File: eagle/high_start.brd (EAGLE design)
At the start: 100.1 x 80.8 mm, 34 parts, among them IC1 7805L, Q1 16Mhz, Q2 IRF510, Q3 IRF510, Q4 IRF510, U2 ATMEGA328P_PDIP

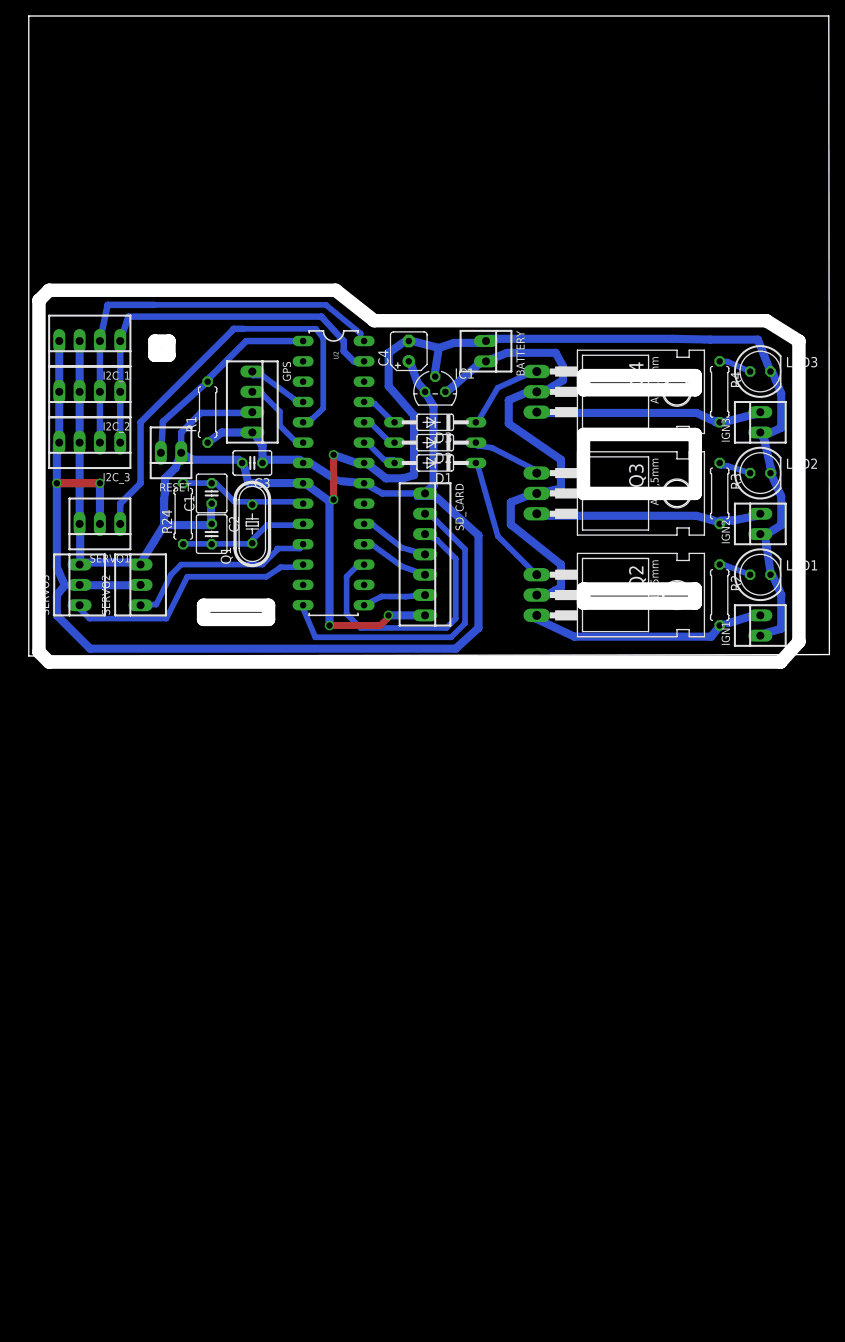
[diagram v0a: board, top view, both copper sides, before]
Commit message: pulldown resistors onto schemo
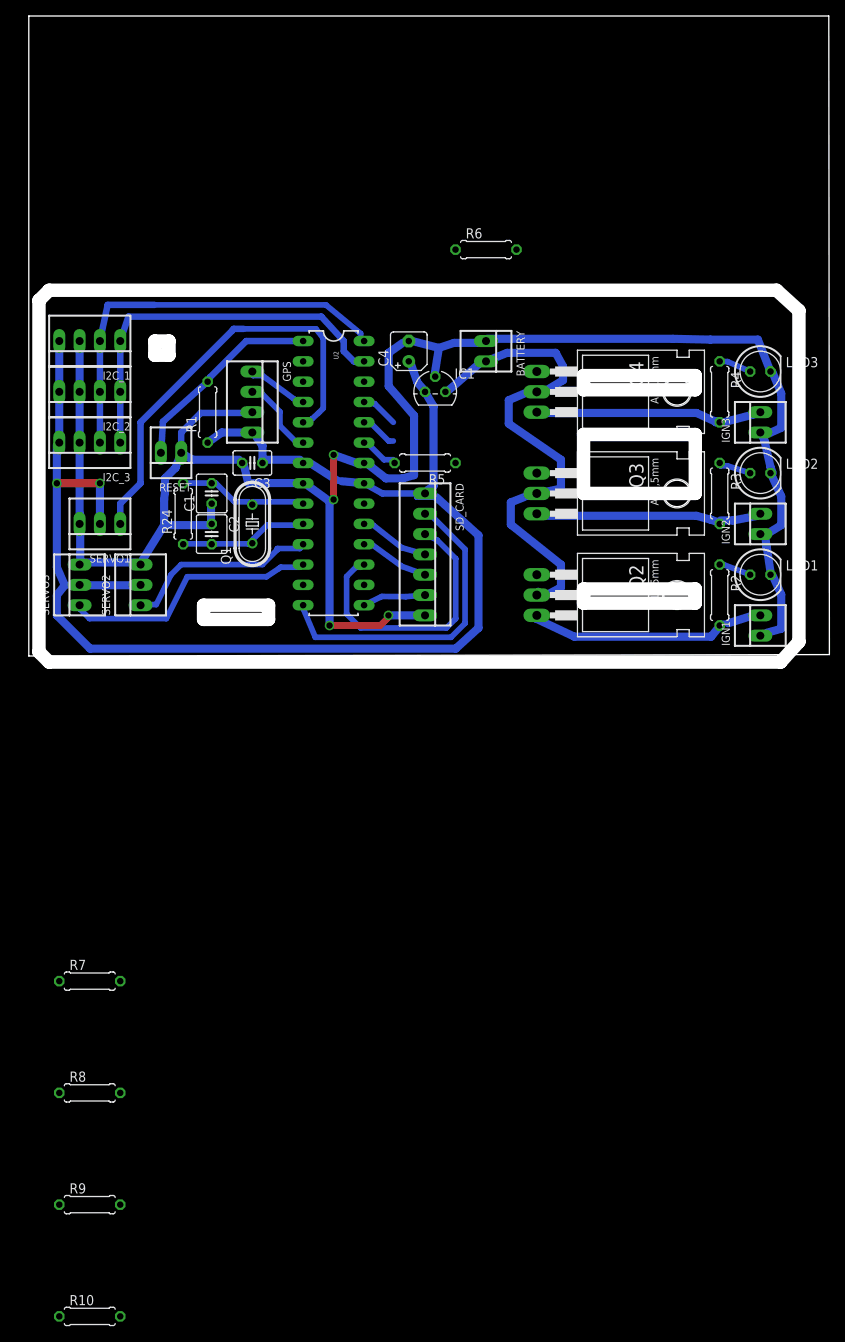
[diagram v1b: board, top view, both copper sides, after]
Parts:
- removed D1, D2, D3: 1N4148DO35-10, diode:DO35-10
- added R10, R6, R9: 10k, rcl:0207/7
- added R5, R7, R8: 220, rcl:0207/7
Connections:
- net GND: now also R10.2, R6.2, R9.2
- net N$12: now also Q2.1, R5.1; no longer D2.C, Q3.1
- net N$13: now also Q3.1, R7.1; no longer D1.C, Q2.1
- net N$14: now also R8.1; no longer D3.C
- net N$18: now also R10.1, R5.2; no longer D1.A
- net N$19: now also R7.2, R9.1; no longer D2.A
- net N$20: now also R6.1, R8.2; no longer D3.A
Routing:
- net N$13: track 16.5 -> 0.00 mm
- net N$14: track 10.5 -> 0.00 mm
- net N$12: track 8.75 -> 0.00 mm
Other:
- outline, holes or cut-outs redrawn
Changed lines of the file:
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@@
 <?xml version="1.0" encoding="utf-8"?>
 <!DOCTYPE eagle SYSTEM "eagle.dtd">
-<eagle version="7.6.0">
+<eagle version="7.7.0">
 <drawing>
 <settings>
@@
 <wire x1="2.54" y1="-0.762" x2="93.98" y2="-0.762" width="1.6764" layer="46"/>
 <wire x1="93.98" y1="-0.762" x2="96.266" y2="1.778" width="1.6764" layer="46"/>
-<wire x1="96.266" y1="1.778" x2="96.266" y2="39.37" width="1.6764" layer="46"/>
-<wire x1="96.266" y1="39.37" x2="92.202" y2="41.91" width="1.6764" layer="46"/>
-<wire x1="92.202" y1="41.91" x2="43.18" y2="41.91" width="1.6764" layer="46"/>
-<wire x1="43.18" y1="41.91" x2="38.354" y2="45.72" width="1.6764" layer="46"/>
-<wire x1="38.354" y1="45.72" x2="2.54" y2="45.72" width="1.6764" layer="46"/>
+<wire x1="96.266" y1="1.778" x2="96.266" y2="43.18" width="1.6764" layer="46"/>
+<wire x1="96.266" y1="43.18" x2="93.472" y2="45.72" width="1.6764" layer="46"/>
+<wire x1="93.472" y1="45.72" x2="2.54" y2="45.72" width="1.6764" layer="46"/>
 <wire x1="1.27" y1="44.45" x2="2.54" y2="45.72" width="1.6764" layer="46"/>
 <wire x1="69.342" y1="27.686" x2="69.342" y2="20.32" width="1.6764" layer="46"/>
@@
 <element name="Q2" library="transistor-fet" package="TO220" value="IRF510" x="69.85" y="7.62" rot="R270"/>
 <element name="Q3" library="transistor-fet" package="TO220" value="IRF510" x="69.85" y="20.32" rot="R270"/>
-<element name="D1" library="diode" package="DO35-10" value="1N4148DO35-10" x="50.8" y="24.13" rot="R180"/>
-<element name="D2" library="diode" package="DO35-10" value="1N4148DO35-10" x="50.8" y="26.67" rot="R180"/>
 <element name="Q4" library="transistor-fet" package="TO220" value="IRF510" x="69.85" y="33.02" rot="R270"/>
-<element name="D3" library="diode" package="DO35-10" value="1N4148DO35-10" x="50.8" y="29.21" rot="R180"/>
 <element name="SERVO1" library="con-molex" package="22-23-2031" value="22-23-2031" x="8.89" y="16.51" rot="R180">
 <attribute name="OC_NEWARK" value="30C0862" x="8.89" y="16.51" size="1.778" layer="27" rot="R180" display="off"/>
@@
 <attribute name="OC_FARNELL" value="1462926" x="57.15" y="38.1" size="1.778" layer="27" rot="R270" display="off"/>
 </element>
+<element name="R5" library="rcl" package="0207/7" value="220" x="49.53" y="24.13" rot="R180"/>
+<element name="R6" library="rcl" package="0207/7" value="10k" x="57.15" y="50.8"/>
+<element name="R7" library="rcl" package="0207/7" value="220" x="7.62" y="-40.64"/>
+<element name="R8" library="rcl" package="0207/7" value="220" x="7.62" y="-54.61"/>
+<element name="R9" library="rcl" package="0207/7" value="10k" x="7.62" y="-68.58"/>
+<element name="R10" library="rcl" package="0207/7" value="10k" x="7.62" y="-82.55"/>
 </elements>
 <signals>
@@
 <contactref element="IGN2" pad="1"/>
 <contactref element="IGN3" pad="1"/>
+<contactref element="R6" pad="2"/>
+<contactref element="R9" pad="2"/>
+<contactref element="R10" pad="2"/>
 <wire x1="91.7194" y1="27.4574" x2="91.44" y2="27.94" width="0" layer="19" extent="16-16"/>
 <wire x1="91.44" y1="15.24" x2="91.7194" y2="15.1892" width="0" layer="19" extent="16-16"/>
 <wire x1="91.44" y1="2.54" x2="91.7194" y2="2.921" width="0" layer="19" extent="16-16"/>
+<wire x1="60.96" y1="50.8" x2="57.2516" y2="39.6494" width="0" layer="19" extent="16-16"/>
+<wire x1="11.43" y1="-68.58" x2="37.592" y2="3.81" width="0" layer="19" extent="1-1"/>
+<wire x1="11.43" y1="-82.55" x2="11.43" y2="-68.58" width="0" layer="19" extent="1-1"/>
 </signal>
 <signal name="N$1">
@@
 <wire x1="42.0624" y1="6.4262" x2="41.91" y2="6.35" width="0.7112" layer="16"/>
 <wire x1="47.1424" y1="7.4168" x2="49.53" y2="7.62" width="0.7112" layer="16"/>
-</signal>
-<signal name="N$12">
-<contactref element="Q3" pad="1"/>
-<contactref element="D2" pad="C"/>
-<wire x1="57.8866" y1="26.035" x2="56.0832" y2="26.289" width="0.7112" layer="16"/>
-<wire x1="63.0936" y1="23.368" x2="57.8866" y2="26.035" width="0.7112" layer="16"/>
-<wire x1="56.0832" y1="26.289" x2="55.88" y2="26.67" width="0.7112" layer="16"/>
-<wire x1="63.0936" y1="23.368" x2="63.5" y2="22.86" width="0.7112" layer="16"/>
-</signal>
-<signal name="N$13">
-<contactref element="Q2" pad="1"/>
-<contactref element="D1" pad="C"/>
-<wire x1="58.6232" y1="14.986" x2="56.0832" y2="23.9522" width="0.7112" layer="16"/>
-<wire x1="63.0936" y1="10.5156" x2="58.6232" y2="14.986" width="0.7112" layer="16"/>
-<wire x1="56.0832" y1="23.9522" x2="55.88" y2="24.13" width="0.7112" layer="16"/>
-<wire x1="63.0936" y1="10.5156" x2="63.5" y2="10.16" width="0.7112" layer="16"/>
-</signal>
-<signal name="N$14">
-<contactref element="Q4" pad="1"/>
-<contactref element="D3" pad="C"/>
-<wire x1="58.6232" y1="33.528" x2="56.0832" y2="29.21" width="0.7112" layer="16"/>
-<wire x1="63.0936" y1="35.56" x2="58.6232" y2="33.528" width="0.7112" layer="16"/>
-<wire x1="56.0832" y1="29.21" x2="55.88" y2="29.21" width="0.7112" layer="16"/>
-<wire x1="63.0936" y1="35.56" x2="63.5" y2="35.56" width="0.7112" layer="16"/>
 </signal>
 <signal name="N$15">
@@
 <signal name="N$18">
 <contactref element="U2" pad="23"/>
-<contactref element="D1" pad="A"/>
 <wire x1="44.3992" y1="24.5364" x2="45.5676" y2="24.5364" width="0.7112" layer="16"/>
 <wire x1="42.0624" y1="26.8732" x2="44.3992" y2="24.5364" width="0.7112" layer="16"/>
-<wire x1="45.5676" y1="24.5364" x2="45.72" y2="24.13" width="0.7112" layer="16"/>
 <wire x1="42.0624" y1="26.8732" x2="41.91" y2="26.67" width="0.7112" layer="16"/>
+<contactref element="R5" pad="2"/>
+<contactref element="R10" pad="1"/>
+<wire x1="44.3992" y1="24.5364" x2="3.81" y2="-82.55" width="0" layer="19" extent="16-16"/>
+<wire x1="45.72" y1="24.13" x2="45.5676" y2="24.5364" width="0" layer="19" extent="16-16"/>
 </signal>
 <signal name="N$19">
 <contactref element="U2" pad="24"/>
-<contactref element="D2" pad="A"/>
 <wire x1="44.9834" y1="26.8732" x2="45.5676" y2="26.8732" width="0.7112" layer="16"/>
 <wire x1="42.6466" y1="29.21" x2="44.9834" y2="26.8732" width="0.7112" layer="16"/>
 <wire x1="41.91" y1="29.21" x2="42.6466" y2="29.21" width="0.7112" layer="16"/>
-<wire x1="45.5676" y1="26.8732" x2="45.72" y2="26.67" width="0.7112" layer="16"/>
+<contactref element="R7" pad="2"/>
+<contactref element="R9" pad="1"/>
+<wire x1="11.43" y1="-40.64" x2="44.9834" y2="26.8732" width="0" layer="19" extent="16-16"/>
+<wire x1="3.81" y1="-68.58" x2="11.43" y2="-40.64" width="0" layer="19" extent="1-1"/>
 </signal>
 <signal name="N$20">
 <contactref element="U2" pad="25"/>
-<contactref element="D3" pad="A"/>
 <wire x1="43.2308" y1="31.5468" x2="42.0624" y2="31.5468" width="0.7112" layer="16"/>
 <wire x1="45.5676" y1="29.21" x2="43.2308" y2="31.5468" width="0.7112" layer="16"/>
 <wire x1="42.0624" y1="31.5468" x2="41.91" y2="31.75" width="0.7112" layer="16"/>
-<wire x1="45.5676" y1="29.21" x2="45.72" y2="29.21" width="0.7112" layer="16"/>
+<contactref element="R8" pad="2"/>
+<contactref element="R6" pad="1"/>
+<wire x1="43.2308" y1="31.5468" x2="53.34" y2="50.8" width="0" layer="19" extent="16-16"/>
+<wire x1="11.43" y1="-54.61" x2="45.5676" y2="29.21" width="0" layer="19" extent="16-16"/>
 </signal>
 <signal name="N$21">
@@
 <wire x1="85.8774" y1="29.21" x2="86.36" y2="29.21" width="1.016" layer="16"/>
 </signal>
+<signal name="N$12">
+<contactref element="Q2" pad="1"/>
+<contactref element="R5" pad="1"/>
+<wire x1="63.5" y1="10.16" x2="53.34" y2="24.13" width="0" layer="19" extent="1-1"/>
+</signal>
+<signal name="N$13">
+<contactref element="Q3" pad="1"/>
+<contactref element="R7" pad="1"/>
+<wire x1="3.81" y1="-40.64" x2="63.5" y2="22.86" width="0" layer="19" extent="1-1"/>
+</signal>
+<signal name="N$14">
+<contactref element="Q4" pad="1"/>
+<contactref element="R8" pad="1"/>
+<wire x1="3.81" y1="-54.61" x2="63.5" y2="35.56" width="0" layer="19" extent="1-1"/>
+</signal>
 </signals>

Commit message: pulldowns placed
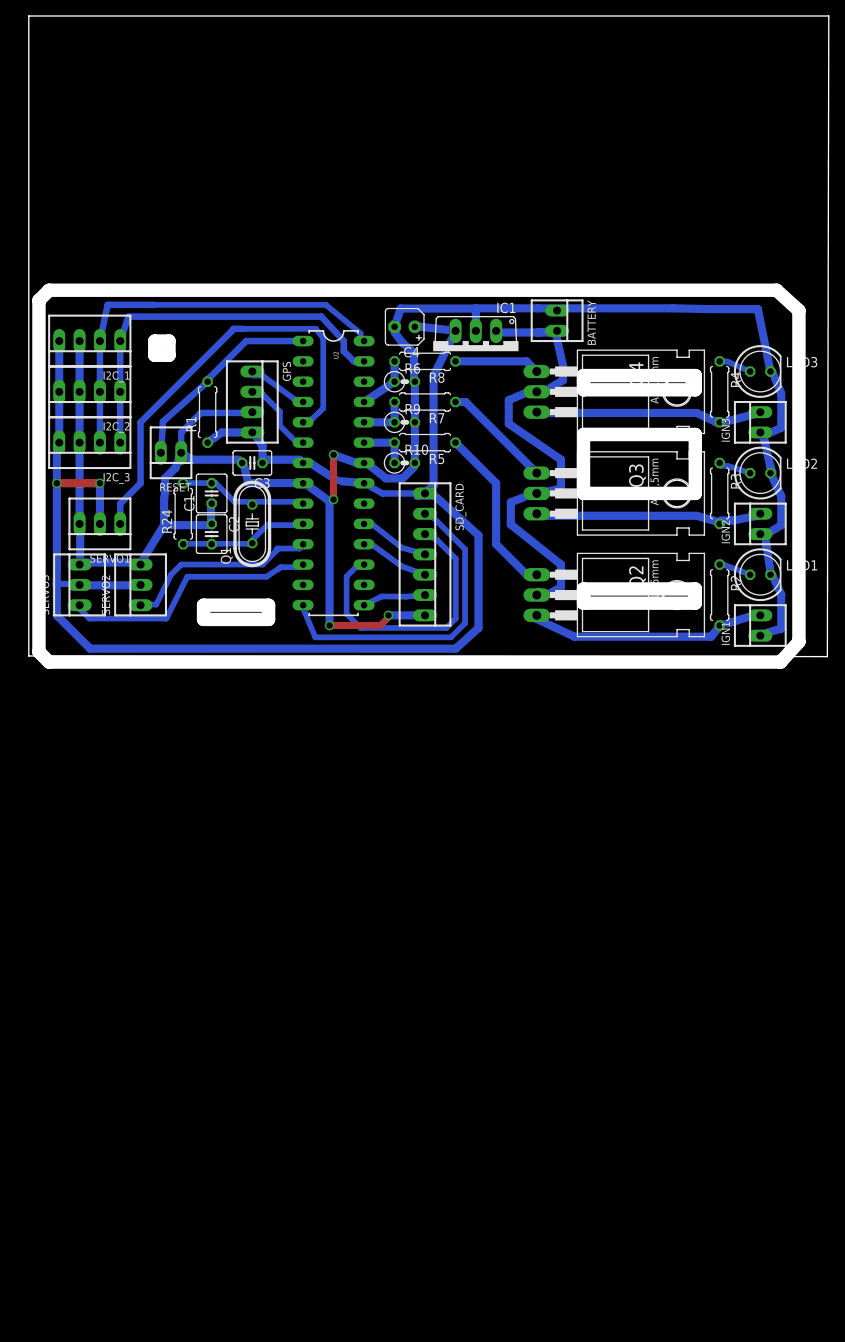
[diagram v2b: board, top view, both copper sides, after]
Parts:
- IC1: value 7805L -> 7805TV; device linear:TO92 -> linear:TO220V
- R10, R6, R9: device rcl:0207/7 -> rcl:0207/2V
- moved R10 113.7 mm to (47.0, 24.1)
- moved R9 105.4 mm to (47.0, 29.2)
- moved R8 100.6 mm to (49.5, 36.8), turned to 180 degrees
- moved R7 83.6 mm to (49.5, 31.8), turned to 180 degrees
- moved R6 19.4 mm to (47.0, 34.3)
- moved BATTERY 9.67 mm to (66.0, 41.9)
- moved IC1 7.18 mm to (55.9, 38.1), turned to 180 degrees
- moved C4 3.09 mm to (47.0, 41.1), turned to 180 degrees
- moved R5 2.54 mm to (49.5, 26.7)
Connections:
- net +5V: now also IC1.3; no longer IC1.1
- net +9V: now also IC1.1; no longer IC1.3
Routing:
- net N$12: track 0.00 -> 21.5 mm
- net N$13: track 0.00 -> 13.8 mm
- net N$14: track 0.00 -> 10.7 mm
- net +5V: track 184.3 -> 194.4 mm
- net GND: track 252.5 -> 260.1 mm
- net +9V: track 65.2 -> 62.4 mm
- net N$20: track 4.73 -> 7.12 mm
- net N$19: track 4.63 -> 6.35 mm
- net N$18: track 4.73 -> 6.35 mm
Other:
- board size 100.1 x 80.8 mm -> 100 x 80.8 mm

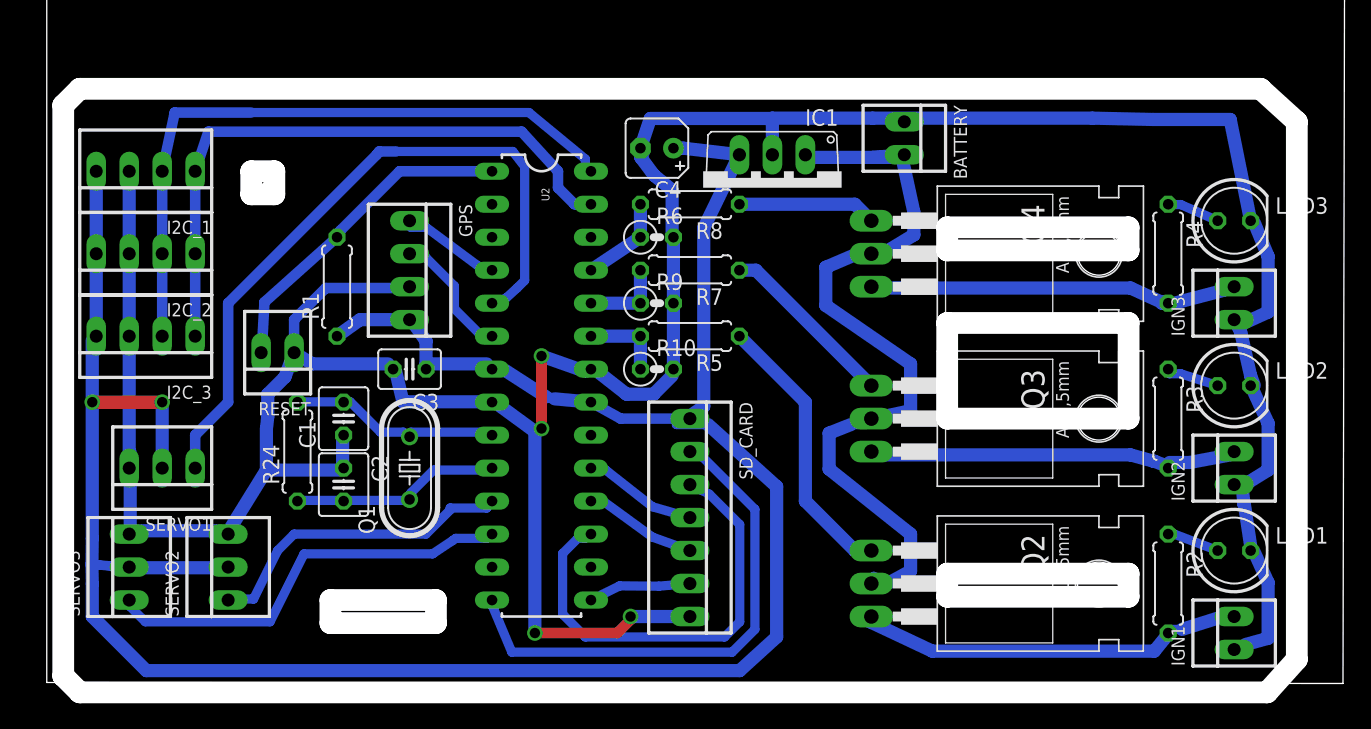
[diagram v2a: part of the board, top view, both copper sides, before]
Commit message: moved fets up to Vbatt for igniter5 worky
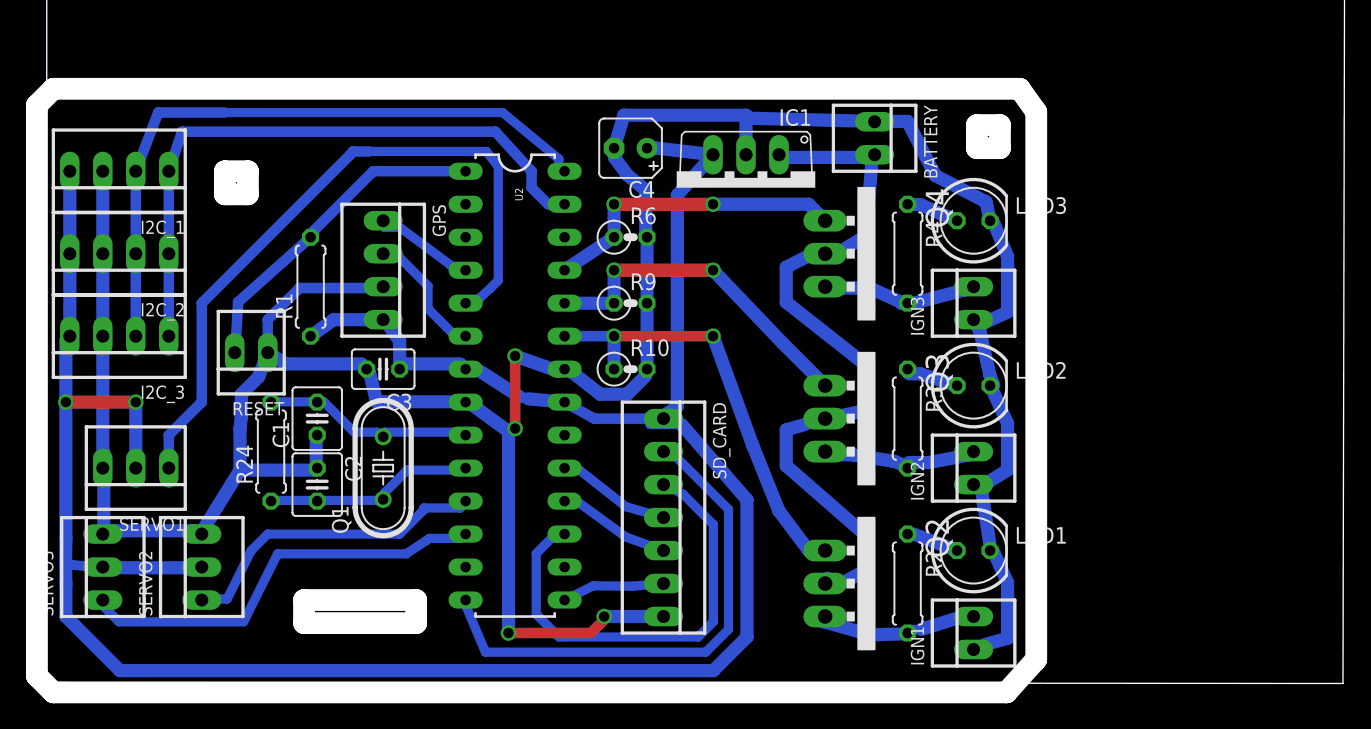
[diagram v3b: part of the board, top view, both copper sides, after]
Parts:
- removed R5, R7, R8: 220, rcl:0207/7
- moved IGN1 20.1 mm to (71.4, 3.81)
- moved IGN2 20.1 mm to (71.4, 16.5)
- moved IGN3 20.1 mm to (71.4, 29.2)
- moved LED1 20.1 mm to (71.4, 10.2)
- moved LED2 20.1 mm to (71.4, 22.9)
- moved LED3 20.1 mm to (71.4, 35.6)
- moved R2 20.1 mm to (66.3, 7.62)
- moved R3 20.1 mm to (66.3, 20.3)
- moved R4 20.1 mm to (66.3, 33.0)
- moved Q2 3.56 mm to (66.3, 7.62)
- moved Q3 3.56 mm to (66.3, 20.3)
- moved Q4 3.56 mm to (66.3, 33.0)
- moved BATTERY 2.29 mm to (63.8, 41.9)
- moved C4 2.03 mm to (45.0, 41.1)
- moved IC1 2.03 mm to (53.8, 38.1)
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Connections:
- removed net N$12: Q2.1, R5.1
- removed net N$13: Q3.1, R7.1
- removed net N$14: Q4.1, R8.1
- net N$18: now also Q2.1; no longer R5.2
- net N$19: now also Q3.1; no longer R7.2
- net N$20: now also Q4.1; no longer R8.2
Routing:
- net N$18: track 6.35 -> 33.4 mm, vias 0 -> 2
- net N$12: track 21.5 -> 0.00 mm
- net GND: track 260.1 -> 239.5 mm
- net N$19: track 6.35 -> 26.4 mm, vias 0 -> 2
- net N$24: track 30.4 -> 12.9 mm
- net N$20: track 7.12 -> 23.9 mm, vias 0 -> 2
- net N$25: track 28.8 -> 12.3 mm
- net N$26: track 28.6 -> 12.1 mm
- net N$13: track 13.8 -> 0.00 mm
- net N$14: track 10.7 -> 0.00 mm
- net +9V: track 62.4 -> 59.4 mm
- net N$1: track 51.4 -> 50.8 mm
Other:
- board size 100 x 80.8 mm -> 100.8 x 80.8 mm
